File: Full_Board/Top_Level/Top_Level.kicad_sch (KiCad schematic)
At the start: 29 parts

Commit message: Add files via upload
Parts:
- removed A? (x2): Pololu_Breakout_A4988, Module:Pololu_Breakout-16_15.2x20.3mm, symbol Driver_Motor:Pololu_Breakout_A4988
- removed C? (x6): C, symbol Device:C
- removed D? (x3): LED, symbol Device:LED
- removed R? (x9): R, symbol Device:R
- removed SW? (x4): SW_Push, symbol Switch:SW_Push
- removed SW?: RotaryEncoder_Switch, symbol Device:RotaryEncoder_Switch
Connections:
- net GND: no longer C?.2
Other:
- added sheet Buttons_All (../Buttons/Buttons_Full.kicad_sch)
- added sheet LEDs_All (../LEDs/LED_Full.kicad_sch)
- added sheet Motor_All (../Motors/Motor_Subsystem.kicad_sch)

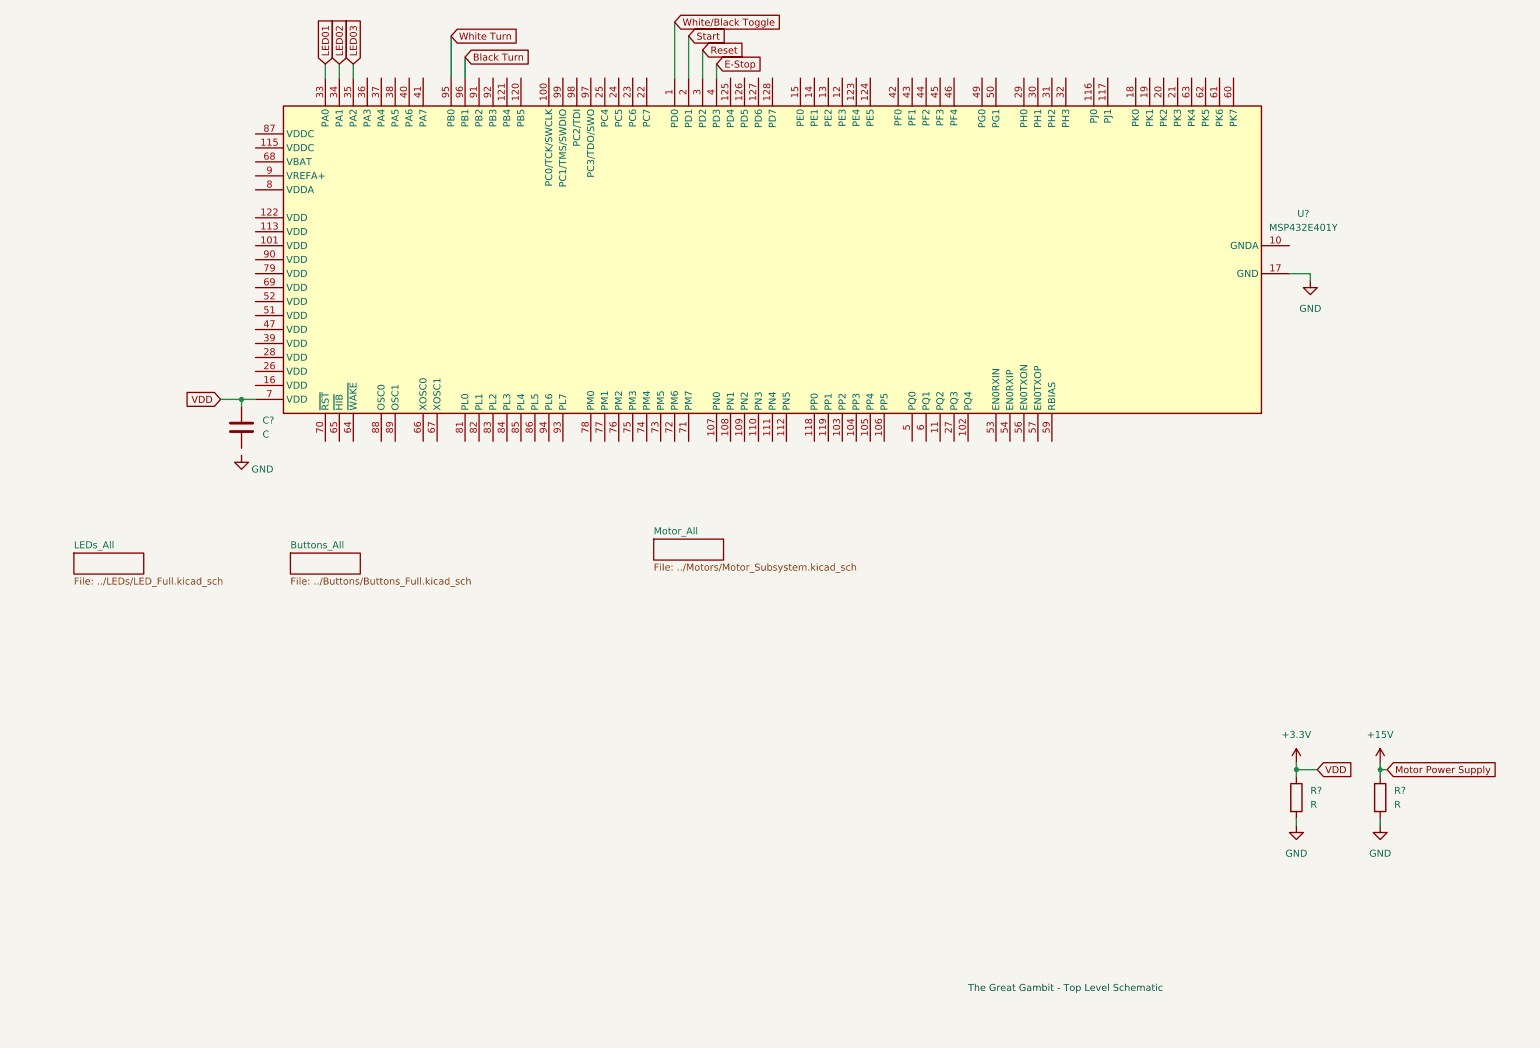
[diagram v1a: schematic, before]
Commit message: Break top level scheamtic into subsystems. Use DRV8824-Q1 driver chip. Document setup
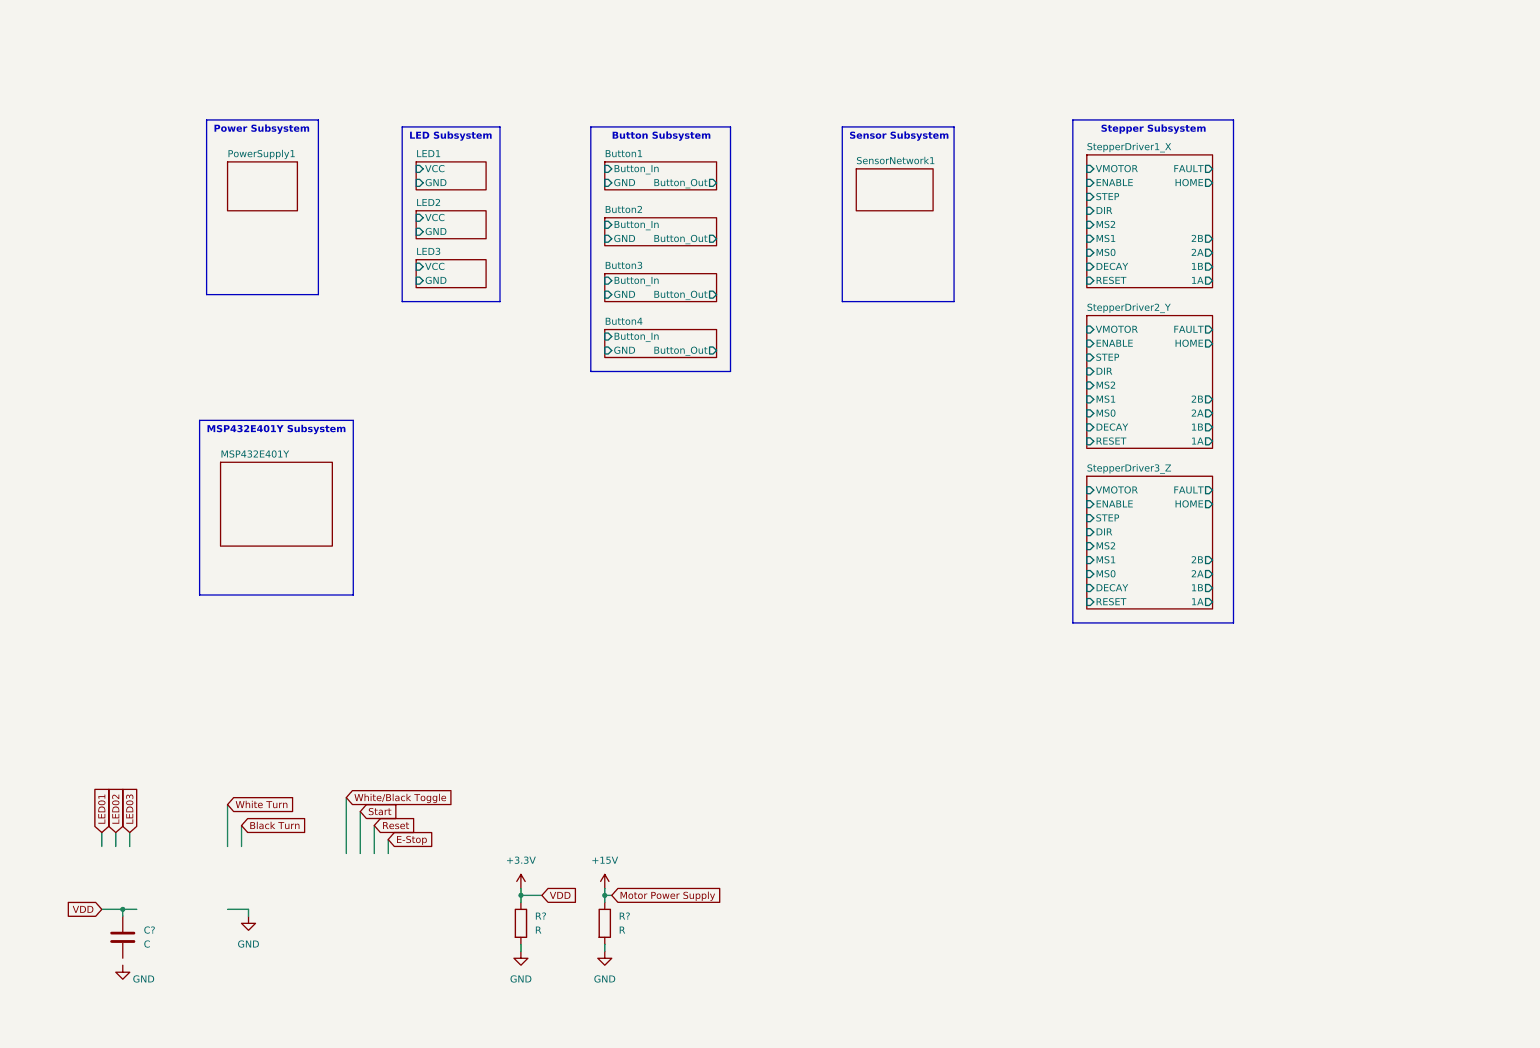
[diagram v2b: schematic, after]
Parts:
- removed U?: MSP432E401Y, Package_QFP:LQFP-128_14x14mm_P0.4mm, symbol MCU_Texas:MSP432E401Y
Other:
- removed sheet Buttons_All
- removed sheet LEDs_All
- removed sheet Motor_All
- added sheet Button1 (../Button_Subsystem/Button.kicad_sch)
- added sheet Button2 (../Button_Subsystem/Button.kicad_sch)
- added sheet Button3 (../Button_Subsystem/Button.kicad_sch)
- added sheet Button4 (../Button_Subsystem/Button.kicad_sch)
- added sheet LED1 (../LED_Subsystem/LED.kicad_sch)
- added sheet LED2 (../LED_Subsystem/LED.kicad_sch)
- added sheet LED3 (../LED_Subsystem/LED.kicad_sch)
- added sheet MSP432E401Y (../MSP_Subsystem/MSP432E401Y.kicad_sch)
- added sheet PowerSupply1 (../Power_Subsystem/PowerSupply.kicad_sch)
- added sheet SensorNetwork1 (../Sensor_Subsystem/SensorNetwork.kicad_sch)
- added sheet StepperDriver1_X (../Stepper_Subsystem/Stepper_Driver.kicad_sch)
- added sheet StepperDriver2_Y (../Stepper_Subsystem/Stepper_Driver.kicad_sch)
- added sheet StepperDriver3_Z (../Stepper_Subsystem/Stepper_Driver.kicad_sch)
- note added: "Button Subsystem"
- note added: "LED Subsystem"
- note added: "MSP432E401Y Subsystem"
- note added: "Power Subsystem"
- note added: "Sensor Subsystem"
- note added: "Stepper Subsystem"
- note removed: "The Great Gambit - Top Level Schematic"
- company: (none) -> The Great Gambit
- title: (none) -> Top Level Schematic
- moved on the sheet: C?, R?
